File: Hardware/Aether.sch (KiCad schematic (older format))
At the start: 3 parts, among them J1 PRGM

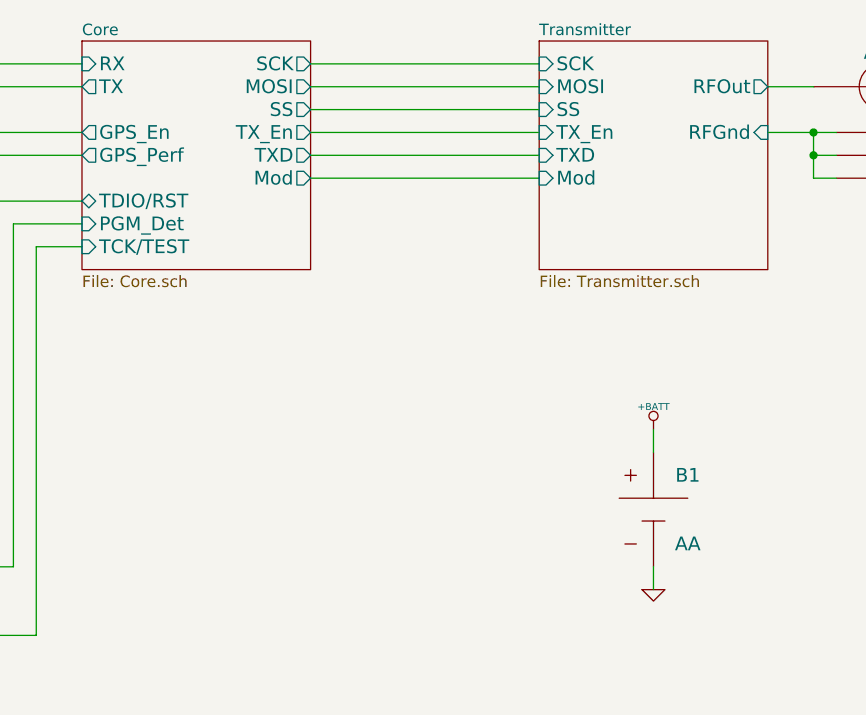
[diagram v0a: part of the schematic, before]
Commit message: Change to 28 pin MCU
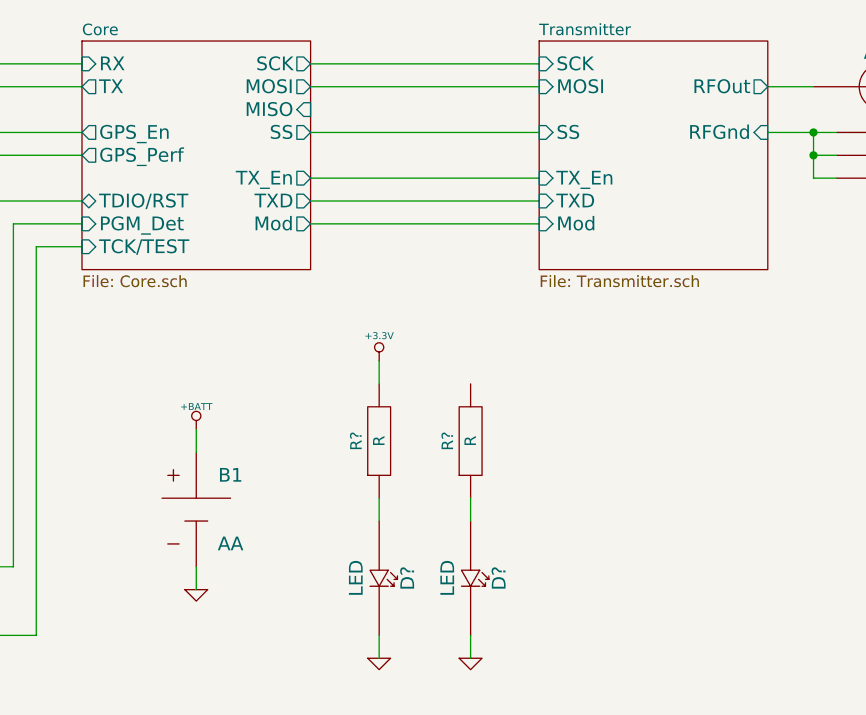
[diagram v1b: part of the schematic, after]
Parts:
- added D? (x2): LED, ~, symbol LED
- added R? (x2): R, ~, symbol R
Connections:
- net GND: now also D?.2, D?.2
- new net: D?.1, R?.1 (x2)
- new net +3.3V: R?.2
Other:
- moved on the sheet: B1
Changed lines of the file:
@@
 F4 "SCK" I L 7200 2900 60
 F5 "MOSI" I L 7200 3000 60
-F6 "SS" I L 7200 3100 60
-F7 "TX_En" I L 7200 3200 60
-F8 "TXD" I L 7200 3300 60
-F9 "Mod" I L 7200 3400 60
+F6 "SS" I L 7200 3200 60
+F7 "TX_En" I L 7200 3400 60
+F8 "TXD" I L 7200 3500 60
+F9 "Mod" I L 7200 3600 60
 $EndSheet
 $Comp
@@
 F5 "MOSI" O R 6200 3000 60
 F6 "SCK" O R 6200 2900 60
-F7 "SS" O R 6200 3100 60
-F8 "TX_En" O R 6200 3200 60
-F9 "TXD" O R 6200 3300 60
-F10 "Mod" O R 6200 3400 60
+F7 "SS" O R 6200 3200 60
+F8 "TX_En" O R 6200 3400 60
+F9 "TXD" O R 6200 3500 60
+F10 "Mod" O R 6200 3600 60
 F11 "TDIO/RST" B L 5200 3500 60
 F12 "TCK/TEST" I L 5200 3700 60
 F13 "PGM_Det" I L 5200 3600 60
 F14 "GPS_Perf" O L 5200 3300 60
+F15 "MISO" I R 6200 3100 60
 $EndSheet
 Wire Wire Line
@@
 	6200 3000 7200 3000
 Wire Wire Line
-	6200 3100 7200 3100
-Wire Wire Line
 	6200 3200 7200 3200
-Wire Wire Line
-	6200 3300 7200 3300
-Wire Wire Line
-	6200 3400 7200 3400
 Wire Wire Line
 	4200 2900 5200 2900
@@
 L BATTERY B1
 U 1 1 52EDBE30
-P 7700 4850
-F 0 "B1" H 7850 5000 60  0000 C CNN
-F 1 "AA" H 7850 4700 60  0000 C CNN
-F 2 "BATT-AA-BK92" H 7700 4850 60  0001 C CNN
-F 3 "~" H 7700 4850 60  0000 C CNN
-	1    7700 4850
+P 5700 4850
+F 0 "B1" H 5850 5000 60  0000 C CNN
+F 1 "AA" H 5850 4700 60  0000 C CNN
+F 2 "BATT-AA-BK92" H 5700 4850 60  0001 C CNN
+F 3 "~" H 5700 4850 60  0000 C CNN
+	1    5700 4850
 	1    0    0    -1
 $EndComp
@@
 L GND #PWR?
 U 1 1 52EDBF2F
-P 7700 5200
-F 0 "#PWR?" H 7700 5200 30  0001 C CNN
-F 1 "GND" H 7700 5130 30  0001 C CNN
-F 2 "" H 7700 5200 60  0000 C CNN
-F 3 "" H 7700 5200 60  0000 C CNN
-	1    7700 5200
+P 5700 5200
+F 0 "#PWR?" H 5700 5200 30  0001 C CNN
+F 1 "GND" H 5700 5130 30  0001 C CNN
+F 2 "" H 5700 5200 60  0000 C CNN
+F 3 "" H 5700 5200 60  0000 C CNN
+	1    5700 5200
 	1    0    0    -1
 $EndComp
@@
 L +BATT #PWR?
 U 1 1 52EDBFF2
-P 7700 4500
-F 0 "#PWR?" H 7700 4450 20  0001 C CNN
-F 1 "+BATT" H 7700 4600 30  0000 C CNN
-F 2 "" H 7700 4500 60  0000 C CNN
-F 3 "" H 7700 4500 60  0000 C CNN
-	1    7700 4500
-	1    0    0    -1
-$EndComp
-Wire Wire Line
-	7700 4500 7700 4600
-Wire Wire Line
-	7700 5100 7700 5200
+P 5700 4500
+F 0 "#PWR?" H 5700 4450 20  0001 C CNN
+F 1 "+BATT" H 5700 4600 30  0000 C CNN
+F 2 "" H 5700 4500 60  0000 C CNN
+F 3 "" H 5700 4500 60  0000 C CNN
+	1    5700 4500
+	1    0    0    -1
+$EndComp
+Wire Wire Line
+	5700 4500 5700 4600
+Wire Wire Line
+	5700 5100 5700 5200
 $Comp
 L CONN-6 J1
@@
 Wire Wire Line
 	5200 3300 4200 3300
+Wire Wire Line
+	6200 3400 7200 3400
+Wire Wire Line
+	6200 3500 7200 3500
+Wire Wire Line
+	6200 3600 7200 3600
+$Comp
+L R R?
+U 1 1 52EF8E3F
+P 6500 4550
+F 0 "R?" H 6500 4650 50  0000 C CNN
+F 1 "R" H 6500 4550 50  0000 C CNN
+F 2 "~" H 6500 4550 60  0000 C CNN
+F 3 "~" H 6500 4550 60  0000 C CNN
+F 4 "W" H 6500 4450 50  0001 C CNN "Power"
+F 5 "%" H 6500 4350 50  0001 C CNN "Tolerance"
+	1    6500 4550
+	0    -1   -1   0
+$EndComp
+$Comp
+L LED D?
+U 1 1 52EF8E5A
+P 6500 5150
+F 0 "D?" H 6500 5275 60  0000 C CNN
+F 1 "LED" H 6500 5050 60  0000 C CNN
+F 2 "~" H 6500 5150 60  0000 C CNN
+F 3 "~" H 6500 5150 60  0000 C CNN
+F 4 "V" H 6900 5675 60  0001 C CNN "Voltage"
+F 5 "I" H 7000 5775 60  0001 C CNN "Current"
+	1    6500 5150
+	0    1    1    0
+$EndComp
+$Comp
+L LED D?
+U 1 1 52EF8F5F
+P 6900 5150
+F 0 "D?" H 6900 5275 60  0000 C CNN
+F 1 "LED" H 6900 5050 60  0000 C CNN
+F 2 "~" H 6900 5150 60  0000 C CNN
+F 3 "~" H 6900 5150 60  0000 C CNN
+F 4 "V" H 7300 5675 60  0001 C CNN "Voltage"
+F 5 "I" H 7400 5775 60  0001 C CNN "Current"
+	1    6900 5150
+	0    1    1    0
+$EndComp
+$Comp
+L R R?
+U 1 1 52EF8FE3
+P 6900 4550
+F 0 "R?" H 6900 4650 50  0000 C CNN
+F 1 "R" H 6900 4550 50  0000 C CNN
+F 2 "~" H 6900 4550 60  0000 C CNN
+F 3 "~" H 6900 4550 60  0000 C CNN
+F 4 "W" H 6900 4450 50  0001 C CNN "Power"
+F 5 "%" H 6900 4350 50  0001 C CNN "Tolerance"
+	1    6900 4550
+	0    -1   -1   0
+$EndComp
+$Comp
+L +3.3V #PWR?
+U 1 1 52EF9184
+P 6500 4200
+F 0 "#PWR?" H 6500 4160 30  0001 C CNN
+F 1 "+3.3V" H 6500 4310 30  0000 C CNN
+F 2 "" H 6500 4200 60  0000 C CNN
+F 3 "" H 6500 4200 60  0000 C CNN
+	1    6500 4200
+	1    0    0    -1
+$EndComp
+Wire Wire Line
+	6500 4200 6500 4300
+$Comp
+L GND #PWR?
+U 1 1 52EF9208
+P 6500 5500
+F 0 "#PWR?" H 6500 5500 30  0001 C CNN
+F 1 "GND" H 6500 5430 30  0001 C CNN
+F 2 "" H 6500 5500 60  0000 C CNN
+F 3 "" H 6500 5500 60  0000 C CNN
+	1    6500 5500
+	1    0    0    -1
+$EndComp
+$Comp
+L GND #PWR?
+U 1 1 52EF9217
+P 6900 5500
+F 0 "#PWR?" H 6900 5500 30  0001 C CNN
+F 1 "GND" H 6900 5430 30  0001 C CNN
+F 2 "" H 6900 5500 60  0000 C CNN
+F 3 "" H 6900 5500 60  0000 C CNN
+	1    6900 5500
+	1    0    0    -1
+$EndComp
+Wire Wire Line
+	6900 5500 6900 5400
+Wire Wire Line
+	6500 5400 6500 5500
+Wire Wire Line
+	6500 4800 6500 4900
+Wire Wire Line
+	6900 4800 6900 4900
 $EndSCHEMATC

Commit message: Modulation section values
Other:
- moved on the sheet: B1, D?, R?
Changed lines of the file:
@@
 	8400 3000 8200 3000
 Wire Wire Line
-	8200 3200 8500 3200
+	8200 3200 8400 3200
+Wire Wire Line
+	8400 3200 8500 3200
 Wire Wire Line
 	8500 3300 8400 3300
 Wire Wire Line
-	8400 3200 8400 3400
+	8400 3200 8400 3300
+Wire Wire Line
+	8400 3300 8400 3400
 Connection ~ 8400 3200
 Wire Wire Line
 	8400 3400 8500 3400
 Connection ~ 8400 3300
-$Sheet
-S 5200 2800 1000 1000
-U 52ECD56F
-F0 "Core" 50
-F1 "Core.sch" 50
-F2 "RX" I L 5200 2900 60
-F3 "TX" O L 5200 3000 60
-F4 "GPS_En" O L 5200 3200 60
-F5 "MOSI" O R 6200 3000 60
-F6 "SCK" O R 6200 2900 60
-F7 "SS" O R 6200 3200 60
-F8 "TX_En" O R 6200 3400 60
-F9 "TXD" O R 6200 3500 60
-F10 "Mod" O R 6200 3600 60
-F11 "TDIO/RST" B L 5200 3500 60
-F12 "TCK/TEST" I L 5200 3700 60
-F13 "PGM_Det" I L 5200 3600 60
-F14 "GPS_Perf" O L 5200 3300 60
-F15 "MISO" I R 6200 3100 60
-$EndSheet
 Wire Wire Line
 	6200 2900 7200 2900
@@
 	6200 3200 7200 3200
 Wire Wire Line
-	4200 2900 5200 2900
-Wire Wire Line
-	4200 3000 5200 3000
+	4200 2900 4400 2900
+Wire Wire Line
+	4400 2900 5200 2900
+Wire Wire Line
+	4200 3000 4500 3000
+Wire Wire Line
+	4500 3000 5200 3000
 Wire Wire Line
 	4200 3200 5200 3200
@@
 L BATTERY B1
 U 1 1 52EDBE30
-P 5700 4850
-F 0 "B1" H 5850 5000 60  0000 C CNN
-F 1 "AA" H 5850 4700 60  0000 C CNN
-F 2 "BATT-AA-BK92" H 5700 4850 60  0001 C CNN
-F 3 "~" H 5700 4850 60  0000 C CNN
-	1    5700 4850
+P 7700 4850
+F 0 "B1" H 7850 5000 60  0000 C CNN
+F 1 "AA" H 7850 4700 60  0000 C CNN
+F 2 "BATT-AA-BK92" H 7700 4850 60  0001 C CNN
+F 3 "~" H 7700 4850 60  0000 C CNN
+	1    7700 4850
 	1    0    0    -1
 $EndComp
@@
 L GND #PWR?
 U 1 1 52EDBF2F
-P 5700 5200
-F 0 "#PWR?" H 5700 5200 30  0001 C CNN
-F 1 "GND" H 5700 5130 30  0001 C CNN
-F 2 "" H 5700 5200 60  0000 C CNN
-F 3 "" H 5700 5200 60  0000 C CNN
-	1    5700 5200
+P 7700 5200
+F 0 "#PWR?" H 7700 5200 30  0001 C CNN
+F 1 "GND" H 7700 5130 30  0001 C CNN
+F 2 "" H 7700 5200 60  0000 C CNN
+F 3 "" H 7700 5200 60  0000 C CNN
+	1    7700 5200
 	1    0    0    -1
 $EndComp
@@
 L +BATT #PWR?
 U 1 1 52EDBFF2
-P 5700 4500
-F 0 "#PWR?" H 5700 4450 20  0001 C CNN
-F 1 "+BATT" H 5700 4600 30  0000 C CNN
-F 2 "" H 5700 4500 60  0000 C CNN
-F 3 "" H 5700 4500 60  0000 C CNN
-	1    5700 4500
-	1    0    0    -1
-$EndComp
-Wire Wire Line
-	5700 4500 5700 4600
-Wire Wire Line
-	5700 5100 5700 5200
+P 7700 4500
+F 0 "#PWR?" H 7700 4450 20  0001 C CNN
+F 1 "+BATT" H 7700 4600 30  0000 C CNN
+F 2 "" H 7700 4500 60  0000 C CNN
+F 3 "" H 7700 4500 60  0000 C CNN
+	1    7700 4500
+	1    0    0    -1
+$EndComp
+Wire Wire Line
+	7700 4500 7700 4600
+Wire Wire Line
+	7700 5100 7700 5200
 $Comp
 L CONN-6 J1
@@
 	4100 5100 4100 4800
 Wire Wire Line
-	3900 5100 4900 5100
+	3900 5100 4100 5100
+Wire Wire Line
+	4100 5100 4900 5100
 Wire Wire Line
 	4000 4900 4000 5500
@@
 Connection ~ 4500 3000
 Wire Wire Line
-	4800 5000 4800 3500
-Wire Wire Line
-	4800 3500 5200 3500
-Wire Wire Line
-	4900 5100 4900 3600
-Wire Wire Line
-	4900 3600 5200 3600
-Wire Wire Line
-	5000 5400 5000 3700
-Wire Wire Line
-	5000 3700 5200 3700
+	4800 5000 4800 4000
+Wire Wire Line
+	4900 5100 4900 4100
+Wire Wire Line
+	5000 5400 5000 4200
 Wire Wire Line
 	5200 3300 4200 3300
@@
 L R R?
 U 1 1 52EF8E3F
-P 6500 4550
-F 0 "R?" H 6500 4650 50  0000 C CNN
-F 1 "R" H 6500 4550 50  0000 C CNN
-F 2 "~" H 6500 4550 60  0000 C CNN
-F 3 "~" H 6500 4550 60  0000 C CNN
-F 4 "W" H 6500 4450 50  0001 C CNN "Power"
-F 5 "%" H 6500 4350 50  0001 C CNN "Tolerance"
-	1    6500 4550
+P 7300 4550
+F 0 "R?" H 7300 4650 50  0000 C CNN
+F 1 "R" H 7300 4550 50  0000 C CNN
+F 2 "~" H 7300 4550 60  0000 C CNN
+F 3 "~" H 7300 4550 60  0000 C CNN
+F 4 "W" H 7300 4450 50  0001 C CNN "Power"
+F 5 "%" H 7300 4350 50  0001 C CNN "Tolerance"
+	1    7300 4550
 	0    -1   -1   0
 $EndComp
@@
 L LED D?
 U 1 1 52EF8E5A
-P 6500 5150
-F 0 "D?" H 6500 5275 60  0000 C CNN
-F 1 "LED" H 6500 5050 60  0000 C CNN
-F 2 "~" H 6500 5150 60  0000 C CNN
-F 3 "~" H 6500 5150 60  0000 C CNN
-F 4 "V" H 6900 5675 60  0001 C CNN "Voltage"
-F 5 "I" H 7000 5775 60  0001 C CNN "Current"
-	1    6500 5150
+P 7300 5150
+F 0 "D?" H 7300 5275 60  0000 C CNN
+F 1 "LED" H 7300 5050 60  0000 C CNN
+F 2 "~" H 7300 5150 60  0000 C CNN
+F 3 "~" H 7300 5150 60  0000 C CNN
+F 4 "V" H 7700 5675 60  0001 C CNN "Voltage"
+F 5 "I" H 7800 5775 60  0001 C CNN "Current"
+	1    7300 5150
 	0    1    1    0
 $EndComp
@@
 L +3.3V #PWR?
 U 1 1 52EF9184
-P 6500 4200
-F 0 "#PWR?" H 6500 4160 30  0001 C CNN
-F 1 "+3.3V" H 6500 4310 30  0000 C CNN
-F 2 "" H 6500 4200 60  0000 C CNN
-F 3 "" H 6500 4200 60  0000 C CNN
-	1    6500 4200
-	1    0    0    -1
-$EndComp
-Wire Wire Line
-	6500 4200 6500 4300
+P 7300 4200
+F 0 "#PWR?" H 7300 4160 30  0001 C CNN
+F 1 "+3.3V" H 7300 4310 30  0000 C CNN
+F 2 "" H 7300 4200 60  0000 C CNN
+F 3 "" H 7300 4200 60  0000 C CNN
+	1    7300 4200
+	1    0    0    -1
+$EndComp
+Wire Wire Line
+	7300 4200 7300 4300
 $Comp
 L GND #PWR?
 U 1 1 52EF9208
-P 6500 5500
-F 0 "#PWR?" H 6500 5500 30  0001 C CNN
-F 1 "GND" H 6500 5430 30  0001 C CNN
-F 2 "" H 6500 5500 60  0000 C CNN
-F 3 "" H 6500 5500 60  0000 C CNN
-	1    6500 5500
+P 7300 5500
+F 0 "#PWR?" H 7300 5500 30  0001 C CNN
+F 1 "GND" H 7300 5430 30  0001 C CNN
+F 2 "" H 7300 5500 60  0000 C CNN
+F 3 "" H 7300 5500 60  0000 C CNN
+	1    7300 5500
 	1    0    0    -1
 $EndComp
@@
 	6900 5500 6900 5400
 Wire Wire Line
-	6500 5400 6500 5500
-Wire Wire Line
-	6500 4800 6500 4900
+	7300 5400 7300 5500
+Wire Wire Line
+	7300 4800 7300 4900
 Wire Wire Line
 	6900 4800 6900 4900
+Wire Wire Line
+	4800 4000 5200 4000
+Wire Wire Line
+	4900 4100 5200 4100
+Wire Wire Line
+	5000 4200 5200 4200
+$Sheet
+S 5200 2800 1000 1500
+U 52ECD56F
+F0 "Core" 50
+F1 "Core.sch" 50
+F2 "RX" I L 5200 2900 60
+F3 "TX" O L 5200 3000 60
+F4 "GPS_En" O L 5200 3200 60
+F5 "SCK" O R 6200 2900 60
+F6 "SS" O R 6200 3200 60
+F7 "TX_En" O R 6200 3400 60
+F8 "TXD" O R 6200 3500 60
+F9 "Mod" O R 6200 3600 60
+F10 "TDIO/RST" B L 5200 4000 60
+F11 "TCK/TEST" I L 5200 4200 60
+F12 "PGM_Det" I L 5200 4100 60
+F13 "GPS_Perf" O L 5200 3300 60
+F14 "DATA" O R 6200 3000 60
+F15 "SCL" I R 6200 3100 60
+F16 "Stat" O R 6200 4200 60
+$EndSheet
 $EndSCHEMATC

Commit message: Something changed
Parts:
- gave numbers to parts that had none: 4
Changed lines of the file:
@@
 Sheet 1 4
 Title "Aether - Pico Tracker"
-Date "3 feb 2014"
+Date "4 feb 2014"
 Rev "1"
 Comp "Aerodyne Labs"
@@
 	8400 3000 8200 3000
 Wire Wire Line
-	8200 3200 8400 3200
-Wire Wire Line
-	8400 3200 8500 3200
+	8200 3200 8500 3200
 Wire Wire Line
 	8500 3300 8400 3300
 Wire Wire Line
-	8400 3200 8400 3300
-Wire Wire Line
-	8400 3300 8400 3400
+	8400 3200 8400 3400
 Connection ~ 8400 3200
 Wire Wire Line
@@
 	6200 3200 7200 3200
 Wire Wire Line
-	4200 2900 4400 2900
-Wire Wire Line
-	4400 2900 5200 2900
-Wire Wire Line
-	4200 3000 4500 3000
-Wire Wire Line
-	4500 3000 5200 3000
+	4200 2900 5200 2900
+Wire Wire Line
+	4200 3000 5200 3000
 Wire Wire Line
 	4200 3200 5200 3200
@@
 $EndComp
 $Comp
-L GND #PWR?
+L GND #PWR01
 U 1 1 52EDBF2F
 P 7700 5200
-F 0 "#PWR?" H 7700 5200 30  0001 C CNN
+F 0 "#PWR01" H 7700 5200 30  0001 C CNN
 F 1 "GND" H 7700 5130 30  0001 C CNN
 F 2 "" H 7700 5200 60  0000 C CNN
@@
 $EndComp
 $Comp
-L +BATT #PWR?
+L +BATT #PWR02
 U 1 1 52EDBFF2
 P 7700 4500
-F 0 "#PWR?" H 7700 4450 20  0001 C CNN
+F 0 "#PWR02" H 7700 4450 20  0001 C CNN
 F 1 "+BATT" H 7700 4600 30  0000 C CNN
 F 2 "" H 7700 4500 60  0000 C CNN
@@
 	4100 5100 4100 4800
 Wire Wire Line
-	3900 5100 4100 5100
-Wire Wire Line
-	4100 5100 4900 5100
+	3900 5100 4900 5100
 Wire Wire Line
 	4000 4900 4000 5500
@@
 	3900 4900 4000 4900
 $Comp
-L +5V #PWR?
+L +5V #PWR03
 U 1 1 52EDCABF
 P 4100 4800
-F 0 "#PWR?" H 4100 4890 20  0001 C CNN
+F 0 "#PWR03" H 4100 4890 20  0001 C CNN
 F 1 "+5V" H 4100 4890 30  0000 C CNN
 F 2 "" H 4100 4800 60  0000 C CNN
@@
 $EndComp
 $Comp
-L GND #PWR?
+L GND #PWR04
 U 1 1 52EDCAB9
 P 4000 5500
-F 0 "#PWR?" H 4000 5500 30  0001 C CNN
+F 0 "#PWR04" H 4000 5500 30  0001 C CNN
 F 1 "GND" H 4000 5430 30  0001 C CNN
 F 2 "" H 4000 5500 60  0000 C CNN
@@
 	6200 3600 7200 3600
 $Comp
-L R R?
+L R R2
 U 1 1 52EF8E3F
 P 7300 4550
-F 0 "R?" H 7300 4650 50  0000 C CNN
+F 0 "R2" H 7300 4650 50  0000 C CNN
 F 1 "R" H 7300 4550 50  0000 C CNN
 F 2 "~" H 7300 4550 60  0000 C CNN
@@
 $EndComp
 $Comp
-L LED D?
+L LED D2
 U 1 1 52EF8E5A
 P 7300 5150
-F 0 "D?" H 7300 5275 60  0000 C CNN
+F 0 "D2" H 7300 5275 60  0000 C CNN
 F 1 "LED" H 7300 5050 60  0000 C CNN
 F 2 "~" H 7300 5150 60  0000 C CNN
@@
 $EndComp
 $Comp
-L LED D?
+L LED D1
 U 1 1 52EF8F5F
 P 6900 5150
-F 0 "D?" H 6900 5275 60  0000 C CNN
+F 0 "D1" H 6900 5275 60  0000 C CNN
 F 1 "LED" H 6900 5050 60  0000 C CNN
 F 2 "~" H 6900 5150 60  0000 C CNN
@@
 $EndComp
 $Comp
-L R R?
+L R R1
 U 1 1 52EF8FE3
 P 6900 4550
-F 0 "R?" H 6900 4650 50  0000 C CNN
+F 0 "R1" H 6900 4650 50  0000 C CNN
 F 1 "R" H 6900 4550 50  0000 C CNN
 F 2 "~" H 6900 4550 60  0000 C CNN
@@
 $EndComp
 $Comp
-L +3.3V #PWR?
+L +3.3V #PWR05
 U 1 1 52EF9184
 P 7300 4200
-F 0 "#PWR?" H 7300 4160 30  0001 C CNN
+F 0 "#PWR05" H 7300 4160 30  0001 C CNN
 F 1 "+3.3V" H 7300 4310 30  0000 C CNN
 F 2 "" H 7300 4200 60  0000 C CNN
@@
 	7300 4200 7300 4300
 $Comp
-L GND #PWR?
+L GND #PWR06
 U 1 1 52EF9208
 P 7300 5500
-F 0 "#PWR?" H 7300 5500 30  0001 C CNN
+F 0 "#PWR06" H 7300 5500 30  0001 C CNN
 F 1 "GND" H 7300 5430 30  0001 C CNN
 F 2 "" H 7300 5500 60  0000 C CNN
@@
 $EndComp
 $Comp
-L GND #PWR?
+L GND #PWR07
 U 1 1 52EF9217
 P 6900 5500
-F 0 "#PWR?" H 6900 5500 30  0001 C CNN
+F 0 "#PWR07" H 6900 5500 30  0001 C CNN
 F 1 "GND" H 6900 5430 30  0001 C CNN
 F 2 "" H 6900 5500 60  0000 C CNN

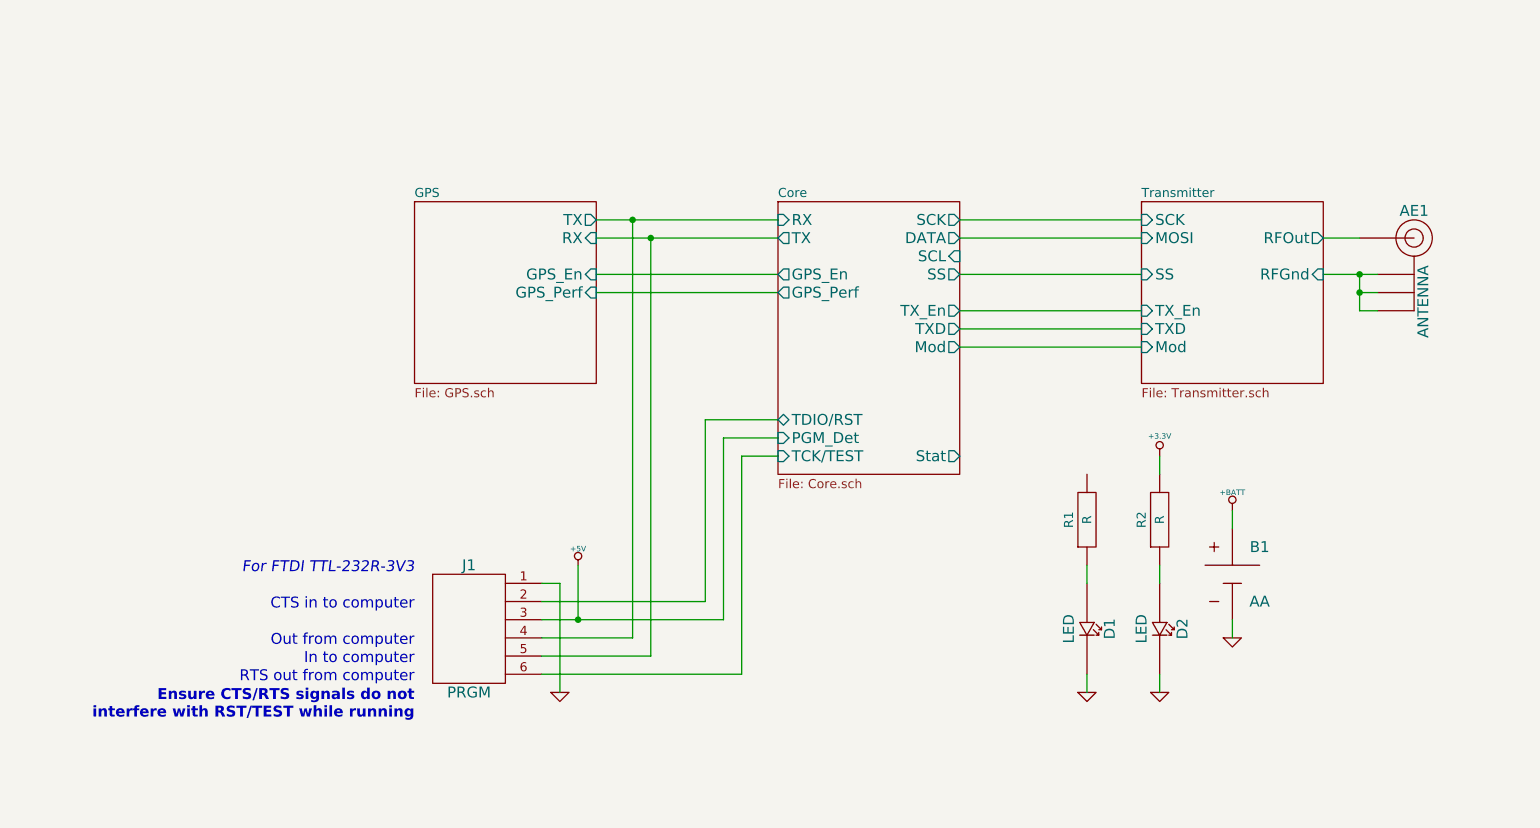
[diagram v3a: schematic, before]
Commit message: Add expansion headers
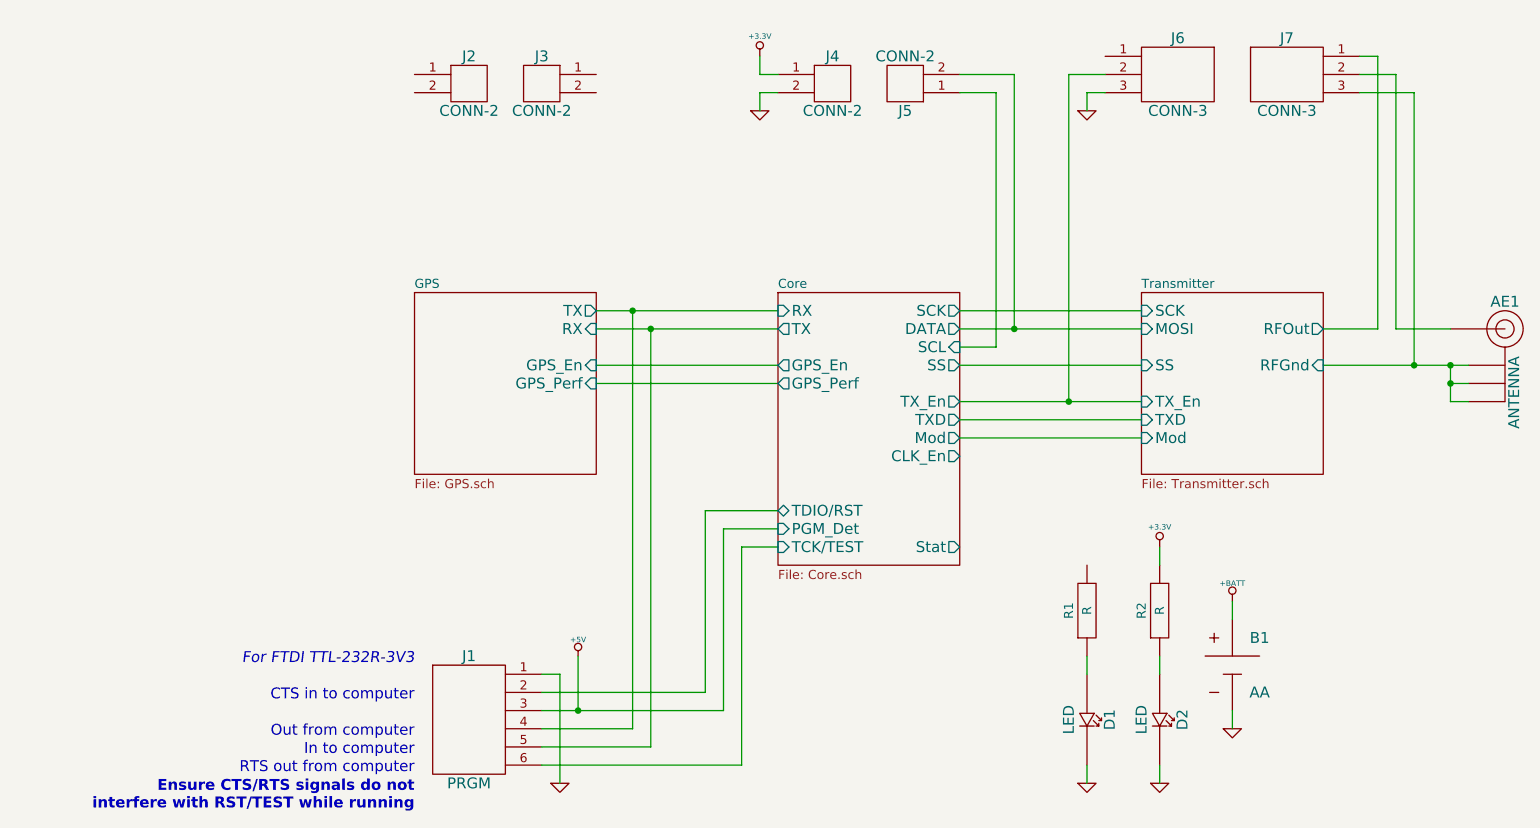
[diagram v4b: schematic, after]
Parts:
- added J2, J3, J4, J5: CONN-2, ~, symbol CONN-2
- added J6, J7: CONN-3, ~, symbol CONN-3
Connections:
- net +3.3V: now also J4.1
- net Core/DATA: now also J5.2
- net Core/SCL: now also J5.1
- net Core/TX_En: now also J6.2
- net GND: now also J4.2, J6.3
- net Transmitter/RFGnd: now also J7.3
- net Transmitter/RFOut: now also J7.1; no longer AE1.P
- new net: AE1.P, J7.2
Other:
- moved on the sheet: AE1, B1, D1, D2, J1, R1, R2
